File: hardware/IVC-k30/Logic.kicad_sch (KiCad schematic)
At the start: 2 parts, among them J4 ATF-JTAG-10, U5 ATF1504AS-10JU84

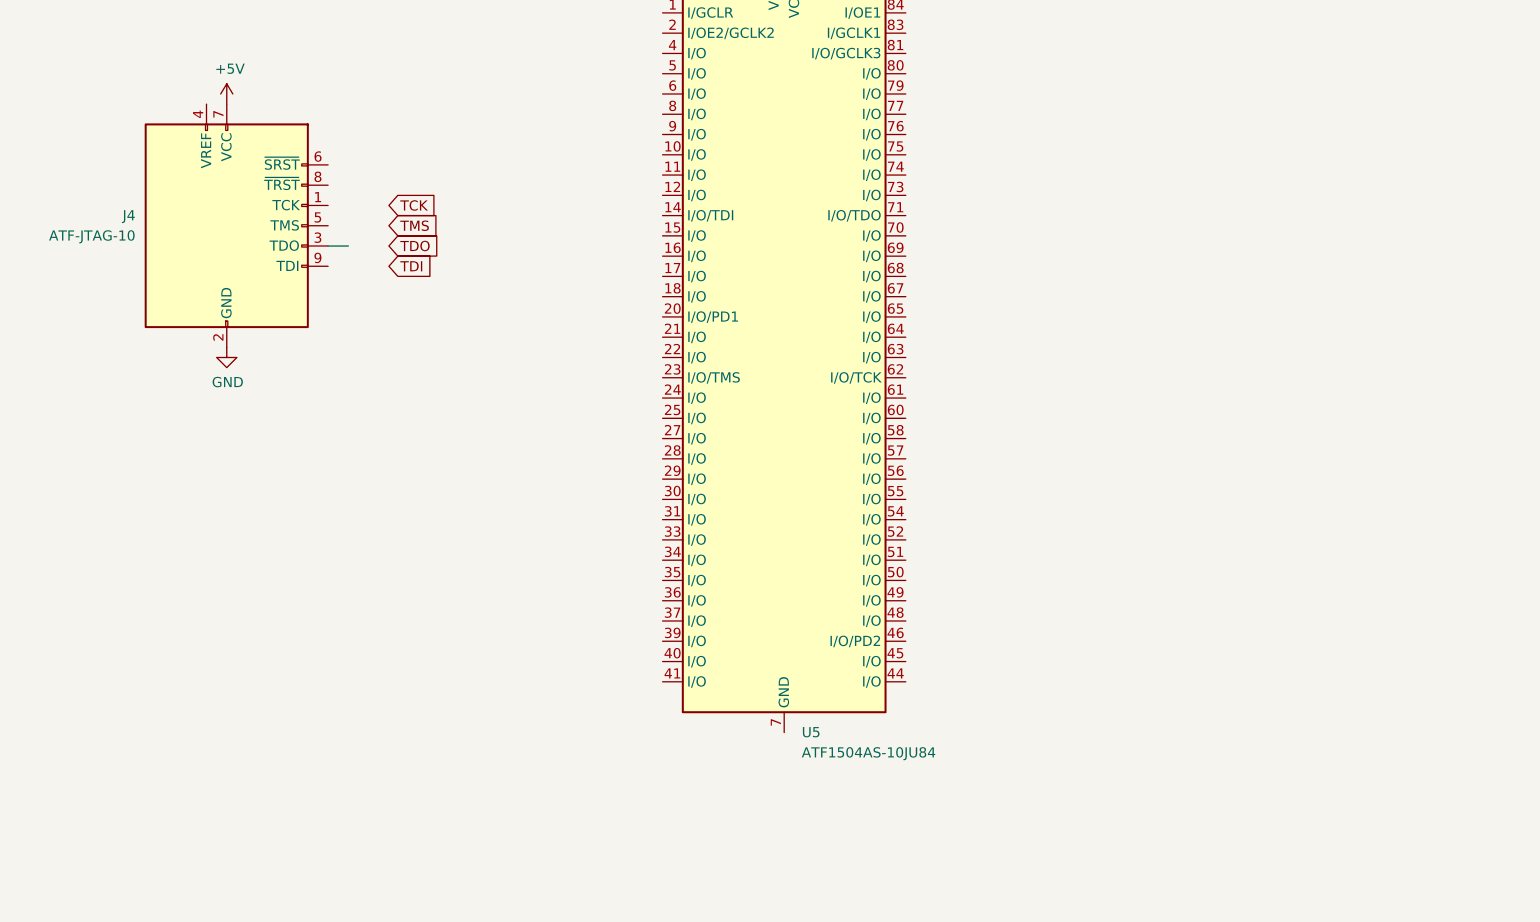
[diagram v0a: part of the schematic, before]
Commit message: Updated k30 CPU card
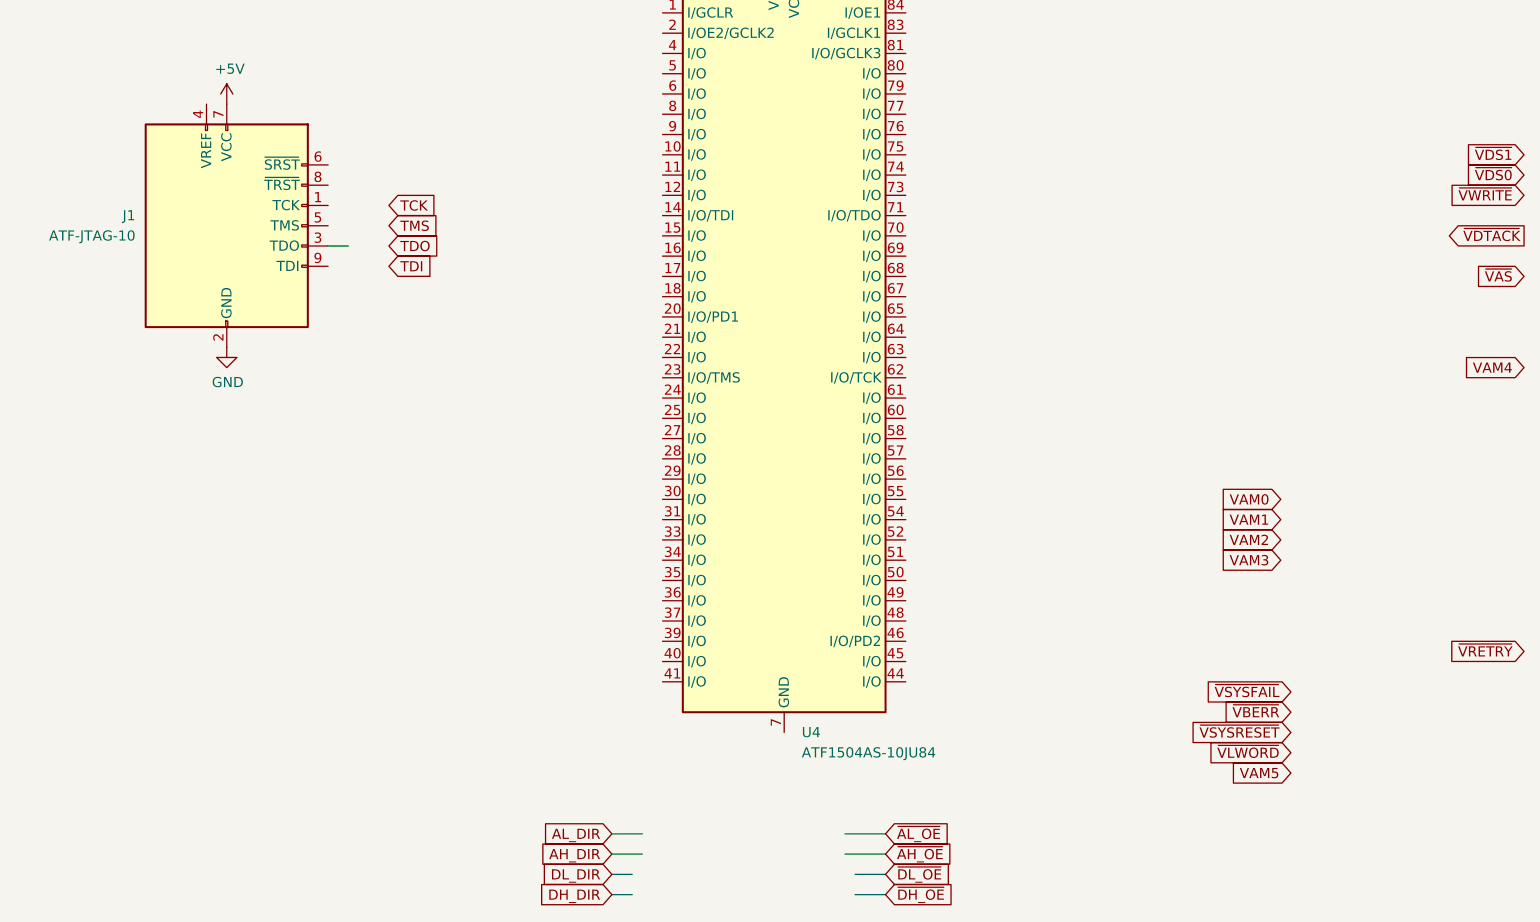
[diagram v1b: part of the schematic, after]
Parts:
- renumbered J4 to J1, U5 to U4

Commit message: Committed changes to k30 board from Oct 9th 2023
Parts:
- added JP1: ROMJMP, Connector_PinHeader_2.54mm:PinHeader_1x03_P2.54mm_Vertical, symbol Jumper:Jumper_3_Bridged12
- added JP6: ENABLE, Jumper:SolderJumper-2_P1.3mm_Open_RoundedPad1.0x1.5mm, symbol Jumper:SolderJumper_2_Open
- added JP7: PULLUP, Jumper:SolderJumper-2_P1.3mm_Bridged_RoundedPad1.0x1.5mm, symbol Jumper:SolderJumper_2_Bridged
- added JP8: ENABLE CFAK, Jumper:SolderJumper-2_P1.3mm_Open_RoundedPad1.0x1.5mm, symbol Jumper:SolderJumper_2_Open
- added R12: 10k, Resistor_THT:R_Axial_DIN0204_L3.6mm_D1.6mm_P5.08mm_Horizontal, symbol Device:R_Small
- added SW2: SW_DIP_x06, Package_DIP:DIP-12_W7.62mm_LongPads, symbol Switch:SW_DIP_x06
- added TP4: ~{DSACK-EXT}, TestPoint:TestPoint_THTPad_2.0x2.0mm_Drill1.0mm, symbol Connector:TestPoint
- added TP8: ~{DSACK-SEL}, TestPoint:TestPoint_THTPad_2.0x2.0mm_Drill1.0mm, symbol Connector:TestPoint
- added U10, U9: 74HC253, Package_SO:SSOP-16_5.3x6.2mm_P0.65mm, symbol 74xx:74LS253
- added U11: 74HC138, Package_SO:TSSOP-16_4.4x5mm_P0.65mm, symbol 74xx:74LS138
- added U12: 74HC393, Package_SO:TSSOP-14_4.4x5mm_P0.65mm, symbol 74xx:74LS393
- added U17: 74LVC1G32, Package_TO_SOT_SMD:SOT-353_SC-70-5_Handsoldering, symbol 74xGxx:74LVC1G32
- added U2: 74HC14, Package_SO:TSSOP-14_4.4x5mm_P0.65mm, symbol 74xx:74HC14
- added U3: 74HC05, Package_SO:TSSOP-14_4.4x5mm_P0.65mm, symbol 74xx:74LS05
- added U4: 74HC139, Package_SO:TSSOP-16_4.4x5mm_P0.65mm, symbol 74xx:74LS139
- added U5: 4072, Package_SO:TSSOP-14_4.4x5mm_P0.65mm, symbol 4xxx:4072
- added U6: 74HC20, Package_SO:TSSOP-14_4.4x5mm_P0.65mm, symbol 74xx:74LS20
- added U7: 74HC32, Package_SO:TSSOP-14_4.4x5mm_P0.65mm, symbol 74xx:74LS32
- added U8: 74HC08, Package_SO:TSSOP-14_4.4x5mm_P0.65mm, symbol 74xx:74LS08
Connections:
- net +5V: now also R12.1, U10.16 (VCC), U10.3 (I3a), U11.16 (VCC), U11.6 (E3), U17.5 (VCC), U9.12 (I2b), U9.13 (I3b), U9.16 (VCC), U9.3 (I3a), U9.4 (I2a), U9.5 (I1a)
- net GND: now also SW2.7, SW2.8, U10.1 (OEa), U10.15 (OEb), U10.8 (GND), U11.8 (GND), U17.3 (GND), U9.1 (OEa), U9.15 (OEb), U9.8 (GND)
- new net: U10.10 (I0b), U4.4 (O0), U8.10
- new net: U10.11 (I1b), U10.6 (I0a), U8.5, U8.8
- new net: U10.12 (I2b), U10.5 (I1a), U8.2, U8.6, U9.10 (I0b)
- new net: U10.13 (I3b), U10.4 (I2a), U8.3, U9.11 (I1b), U9.6 (I0a)
- new net: U4.5 (O1), U8.1
- new net: JP7.2 (B), R12.2
- new net: JP6.1 (A), U3.12
- new net: U17.1, U2.10
- new net: U2.8, U3.11
- new net: SW2.1, U12.4 (Q1)
- new net: SW2.10, SW2.11, SW2.12, U3.13
- new net: SW2.2, U12.5 (Q2)
- new net: SW2.3, U12.6 (Q3)
- new net: SW2.4, U3.6
- new net: U4.7 (O3), U8.9
- new net: U3.9, U6.6
- new net: U5.1, U7.1
- new net: U5.13, U7.2
- new net: U7.3, U7.4
- new net: U4.6 (O2), U8.4
- new net: U11.13 (O2), U8.13
- new net: U11.14 (O1), U8.12
- new net: U11.5 (E2), U7.6
- new net: JP8.2 (B), TP8.1, U12.2 (MR)
- new net: U12.8 (Q3), U3.5
- new net A0: U10.14 (A0), U9.14 (A0)
- new net A1: U10.2 (A1), U9.2 (A1)
- new net A16: U6.13
- new net A20: U11.1 (A0)
- new net A21: U11.2 (A1)
- new net A22: U11.3 (A2)
- new net A23: U7.5
- new net A24: U5.12
- new net A25: U5.11
- new net A26: U5.10
- new net A27: U5.9
- new net A28: U5.5
- new net A29: U5.4
- new net A30: U5.3
- new net A31: U5.2
- new net ATA-READY: U2.11
- new net CLK: U12.1 (CP), U12.13 (CP)
- new net FC0: U6.9
- new net FC1: U6.10
- new net FC2: U6.12
- new net SIZ0: U4.2 (A0)
- new net SIZ1: U4.3 (A1)
- new net ~{0SEL}: JP1.3 (B), U11.15 (O0)
- new net ~{3SEL}: JP1.1 (A), U11.12 (O3)
- new net ~{4SEL}: U11.11 (O4)
- new net ~{5SEL}: U11.10 (O5)
- new net ~{6SEL}: JP8.1 (A), U11.9 (O6), U17.2
- new net ~{AS}: U11.4 (E1), U12.12 (MR)
- new net ~{ATA-DSACK}: U17.4, U6.4
- new net ~{BERR}: SW2.9
- new net ~{CDIS}: SW2.5
- new net ~{DS0}: U10.9 (Zb)
- new net ~{DS1}: U10.7 (Za)
- new net ~{DS2}: U9.9 (Zb)
- new net ~{DS3}: U9.7 (Za)
- new net ~{DSACK-EXT}: JP6.2 (B), JP7.1 (A), TP4.1, U6.5
- new net ~{DSACK0}: U3.8
- new net ~{DSACK1}: U3.10
- new net ~{DS}: U4.1 (E)
- new net ~{IACK}: U6.8
- new net ~{IOSEL}: U11.7 (O7)
- new net ~{MMUDIS}: SW2.6
- new net ~{RAMSEL}: U2.9, U6.1, U8.11
- new net ~{ROMSEL}: JP1.2 (C), U6.2
- no-connect marks 0 -> 4
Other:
- note added: "14"
- note added: "23"
- note added: "BERR GENERATOR"
- note added: "COMPACT FLASH DSACK GENERATOR LOGIC"
- note added: "DSACK ASSERTION LOGIC"
- note added: "DSACK GENERATOR FOR EXTERNAL IO"
- note added: "NEED 28 + 23 + 4 = 55"
- note added: "ROM ADDRESS SELECTION"
